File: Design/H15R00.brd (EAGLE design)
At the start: 34.6 x 30 mm, 21 parts, among them P1 HEXABIT_17.32_NO_P3_P6, U1 STM32F091CBU6, X1 XTALL_CSTCE8M00G52

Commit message: Finished schematics
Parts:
- added AO: 1751248, Hexabitz:CON-PHOENIX-350_1751248
- added C10, C11: 100nF, Hexabitz:C-0603
- added C12, C13: 100pF, Hexabitz:C-0603
- added C14, C15: 10pF, Hexabitz:C-0603
- added C16: 20nF, Hexabitz:C-0603
- added C17: 150pF, Hexabitz:C-0603
- added PWR: 1751251, con-phoenix-350:1751251
- added R4: 71.5R, Hexabitz:R-0603
- added R5: 24.9K, Hexabitz:R-0603
- added R6: 8.25K, Hexabitz:R-0603
- added R7: 12.4K, Hexabitz:R-0603
- added U2: OPA188, Hexabitz:DBV0005A_N
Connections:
- net UART1_RX renamed UART1_RX*
- net UART1_TX renamed UART1_TX*
- net UART2_RX renamed UART2_RX*
- net UART2_TX renamed UART2_TX*
- removed net UART6_RX: U1.P$15
- removed net UART6_TX: U1.P$14
- new net +15V: C11.1, C13.1, C14.1, PWR.3, U2.5
- new net -15V: C10.1, C12.1, C15.1, PWR.1, U2.2
- new net AGND: AO.2, C10.2, C12.2, C14.2, C15.2, C16.2, PWR.2, R7.2
- new net DAC_OUT: U1.P$14, U2.3
- new net N$1: AO.1, C16.1, R4.1
- new net N$10: R5.1
- new net N$11: P1.PAD_PU1
- new net N$12: P1.PAD_PU2
- new net N$13: P1.PAD_PU4
- new net N$14: P1.PAD_PD5
- new net N$15: P1.PAD_PD1
- new net N$16: P1.PAD_PD2
- new net N$17: P1.PAD_PD4
- new net N$18: P1.PAD_PU5
- new net N$2: C17.2, R4.2, U2.1
- new net N$8: C17.1, R5.2, R6.1, R7.1, U2.4
- new net VCC: R6.2
- net VSSA: now also C11.2, C13.2

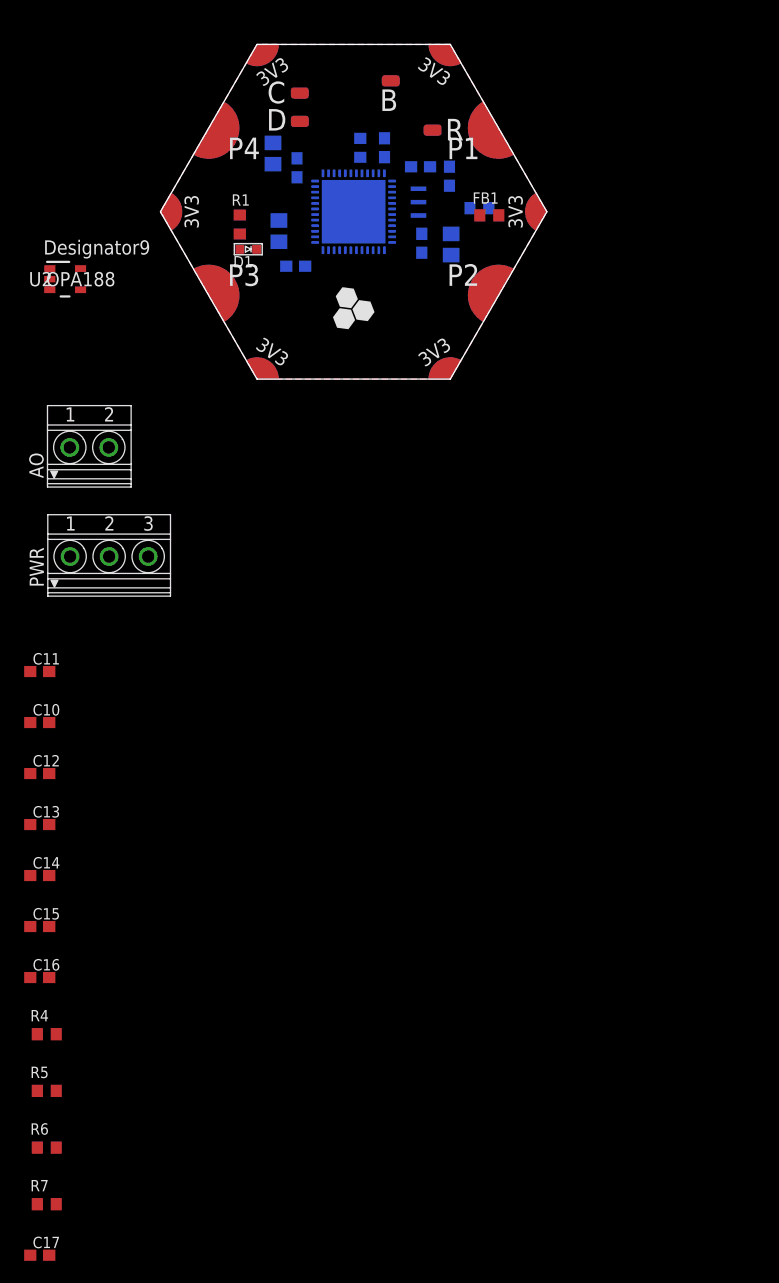
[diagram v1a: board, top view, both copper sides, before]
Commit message: Placed all components Routed analog part and most digital Added VSSA polygon
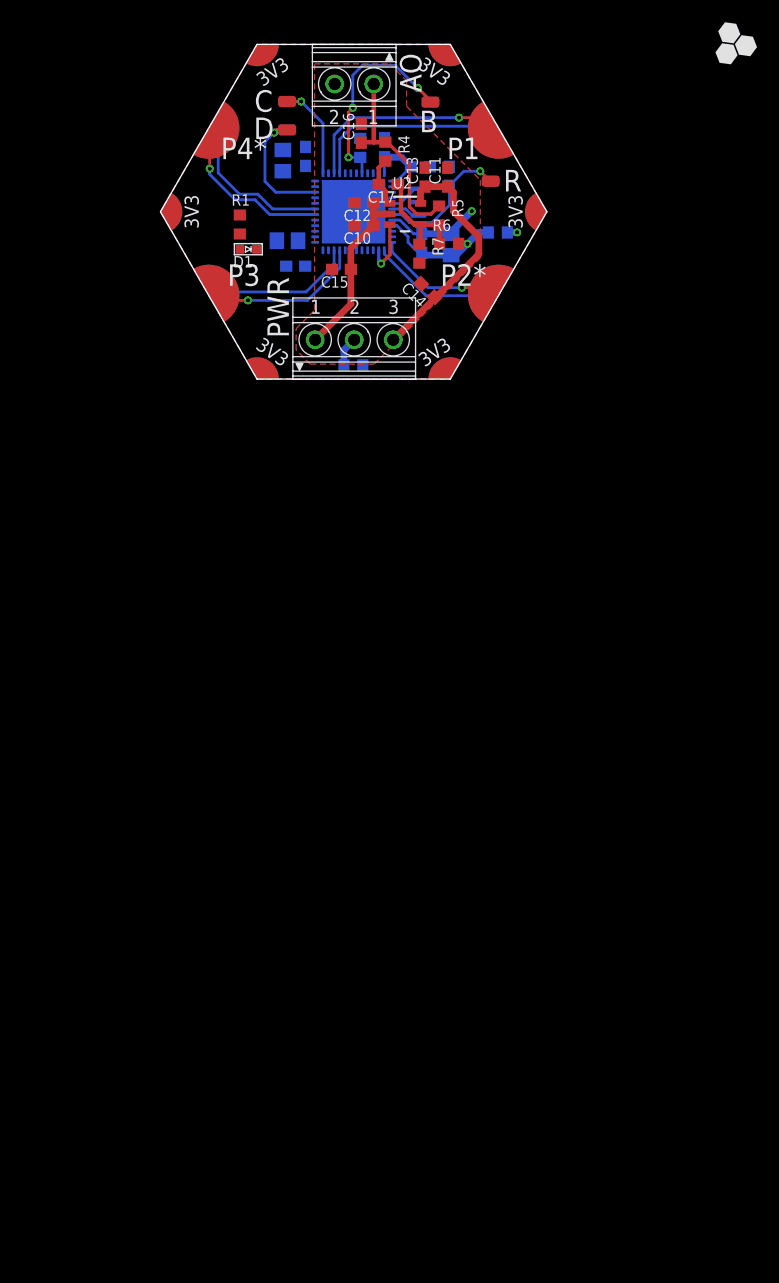
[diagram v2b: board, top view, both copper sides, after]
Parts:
- moved C17 101.0 mm to (37.7, 37.1), turned to 180 degrees
- moved R7 91.5 mm to (40.5, 30.9), turned to 270 degrees
- moved R6 88.7 mm to (43.2, 31.8)
- moved R5 86.0 mm to (42.3, 34.3), turned to 270 degrees
- moved R4 84.7 mm to (37.5, 40.0), turned to 270 degrees
- moved C16 81.0 mm to (35.3, 41.7), turned to 90 degrees
- moved C13 67.5 mm to (41.0, 37.7), turned to 90 degrees
- moved C15 64.8 mm to (33.5, 29.5), turned to 180 degrees
- moved C14 62.9 mm to (41.3, 27.6), turned to 135 degrees
- moved C12 58.9 mm to (35.6, 35.4), turned to 180 degrees
- moved C11 57.5 mm to (43.1, 37.7), turned to 90 degrees
- moved C10 53.2 mm to (35.6, 33.4), turned to 180 degrees
- moved AO 40.2 mm to (34.7, 46.0), turned to 180 degrees
- moved U2 31.0 mm to (39.2, 34.4)
- moved PWR 29.3 mm to (34.7, 23.2)
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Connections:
- removed net AGND: AO.2, C10.2, C12.2, C14.2, C15.2, C16.2, PWR.2, R7.2
- removed net N$10: R5.1
- removed net N$11: P1.PAD_PU1
- removed net N$12: P1.PAD_PU2
- removed net N$13: P1.PAD_PU4
- removed net N$14: P1.PAD_PD5
- removed net N$15: P1.PAD_PD1
- removed net N$16: P1.PAD_PD2
- removed net N$17: P1.PAD_PD4
- removed net N$18: P1.PAD_PU5
- removed net VCC: R6.2
- net N$1: now also R5.1
- net UART1_RX*: now also P1.PAD_PD5
- net UART1_TX*: now also P1.PAD_PU5
- net UART2_RX*: now also P1.PAD_PD2
- net UART2_TX*: now also P1.PAD_PU2
- net UART3_RX: now also P1.PAD_PD4
- net UART3_TX: now also P1.PAD_PU4
- net UART5_RX: now also P1.PAD_PD1
- net UART5_TX: now also P1.PAD_PU1
- net VDDA: now also R6.2
- net VSSA: now also AO.2, C10.2, C12.2, C14.2, C15.2, C16.2, PWR.2, R7.2
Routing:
- net +15V: track 0.00 -> 21.8 mm
- net B1: track 0.00 -> 20.6 mm, vias 0 -> 3
- net UART5_TX: track 0.00 -> 18.7 mm, vias 0 -> 1
- net N$1: track 0.00 -> 17.4 mm
- net UART5_RX: track 0.00 -> 17.4 mm
- net -15V: track 0.00 -> 15.9 mm
- net UART1_TX*: track 0.00 -> 15.0 mm, vias 0 -> 1
- net UART3_TX: track 0.00 -> 14.3 mm, vias 0 -> 1
- net UART1_RX*: track 0.00 -> 13.8 mm
- net R1: track 0.00 -> 13.7 mm, vias 0 -> 1
- net UART3_RX: track 0.00 -> 12.9 mm
- net N$7: track 0.00 -> 12.1 mm, vias 0 -> 1
- net UART2_RX*: track 0.00 -> 11.7 mm
- net VDDA: track 0.00 -> 11.7 mm, vias 0 -> 1
- net VSSA: track 0.00 -> 11.3 mm, vias 0 -> 1
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- added copper zone on layer 1, net VSSA
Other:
- board text added: "P2*"
- board text added: "P4*"
- board text removed: "P2"
- board text removed: "P4"

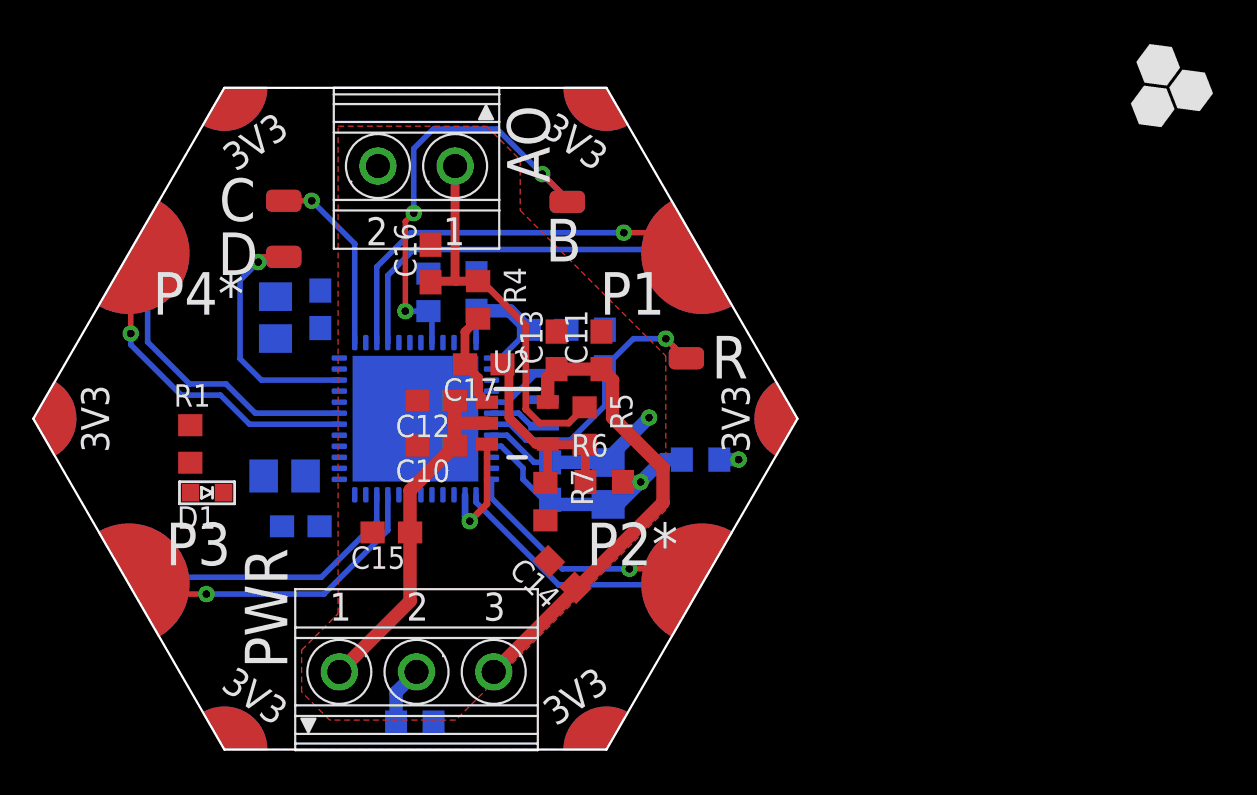
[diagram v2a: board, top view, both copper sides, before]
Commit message: Finished routing and silkscreen
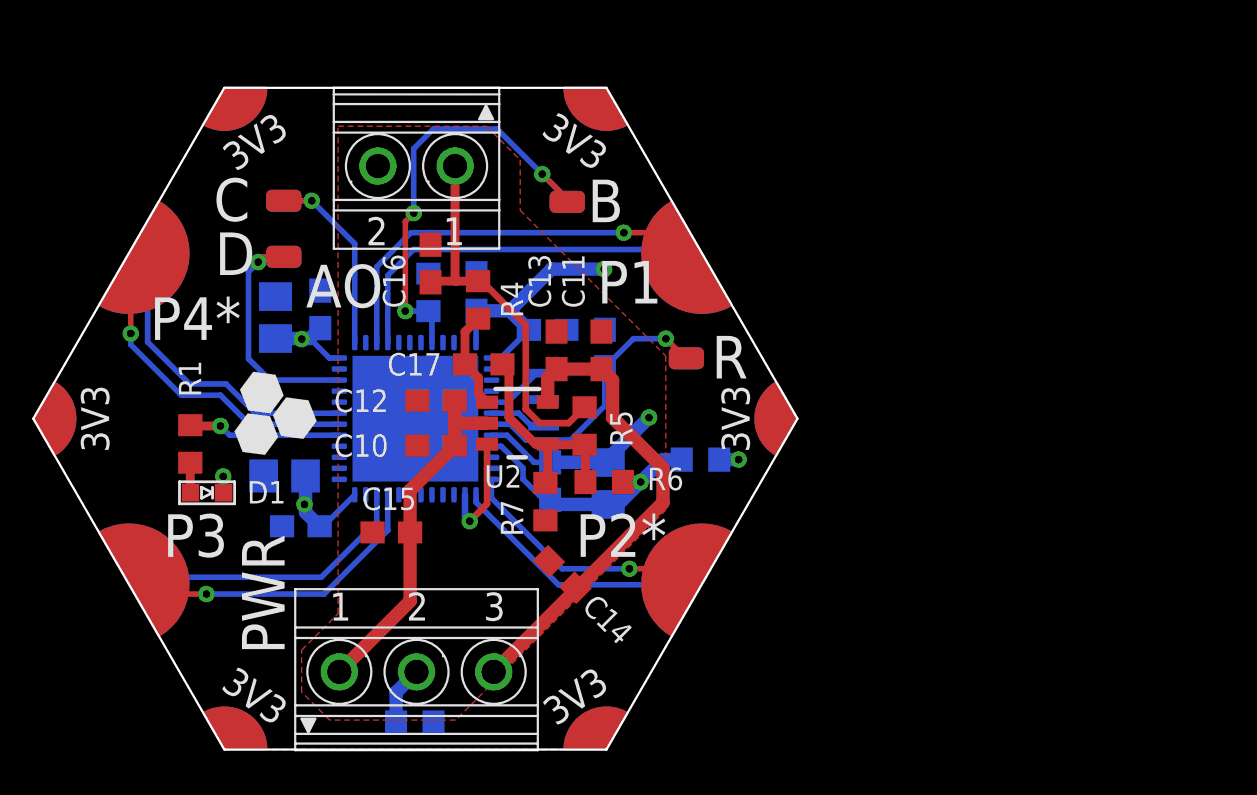
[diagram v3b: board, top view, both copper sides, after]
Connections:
- net GND: now also U1.P$15, U1.P$16, U1.P$17, U1.P$18, U1.P$19, U1.P$2, U1.P$20, U1.P$3, U1.P$32, U1.P$33, U1.P$38, U1.P$4, U1.P$45, U1.P$46
- net N$3: now also U1.P$29; no longer U1.P$32
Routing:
- net VDD: track 7.29 -> 21.0 mm, vias 1 -> 4
- net N$3: track 0.00 -> 6.94 mm, vias 0 -> 1
- net N$4: track 0.00 -> 1.37 mm
- net GND: track 0.00 -> 0.75 mm, vias 0 -> 1
- net N$7: track 12.1 -> 11.6 mm
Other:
- board text added: "+15V"
- board text added: "-10V..10V"
- board text added: "-15V"
- board text added: "AO"

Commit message: Solved DRC Generated gerber, drill, pick n place and schematics Generated BOM First release Ver 0
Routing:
- net VDD: track 21.0 -> 21.7 mm
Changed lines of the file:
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@@
 <attribute name="COMPTYPE" value="IC" x="39.243" y="34.417" size="1.778" layer="27" display="off"/>
 <attribute name="MANUFACTURER" value="Texas Instruments" x="39.243" y="34.417" size="1.778" layer="27" display="off"/>
+<attribute name="MFN" value="Texas Instruments" x="39.243" y="34.417" size="1.778" layer="27" display="off"/>
 <attribute name="MOUNTTYPE" value="SMT" x="39.243" y="34.417" size="1.778" layer="27" display="off"/>
+<attribute name="MPN" value="OPA188AIDBVR" x="39.243" y="34.417" size="1.778" layer="27" display="off"/>
 <attribute name="NAME" x="37.7444" y="31.496" size="1.016" layer="25" rot="SR0"/>
+<attribute name="OCTOPART_URL" value="https://octopart.com/opa188aidbvr-texas+instruments-27810397?r=sp&amp;s=zwpAzK6tSwu39ID1-8lLKg" x="39.243" y="34.417" size="1.778" layer="27" display="off"/>
 <attribute name="PACKAGEREFERENCE" value="DBV0005A" x="39.243" y="34.417" size="1.778" layer="27" display="off"/>
 <attribute name="PARTNUMBER" value="OPA188AIDBVR" x="39.243" y="34.417" size="1.778" layer="27" display="off"/>
@@
 <attribute name="NAME" x="38.493190625" y="30.94939375" size="1.016" layer="25" rot="R270"/>
 <attribute name="OCTOPART_URL" value="https://octopart.com/era-3aeb1242v-panasonic-55639351?r=sp&amp;s=K0xQjqOwSGaT1tqbXnh0hg" x="40.513" y="30.861" size="1.778" layer="27" rot="R270" display="off"/>
-<attribute name="RESISTANCE" value="12.4 Ohm" x="40.513" y="30.861" size="1.778" layer="27" rot="R270" display="off"/>
+<attribute name="RESISTANCE" value="12.4 kOhm" x="40.513" y="30.861" size="1.778" layer="27" rot="R270" display="off"/>
 <attribute name="TOLERANCE" value="0.1%" x="40.513" y="30.861" size="1.778" layer="27" rot="R270" display="off"/>
 <attribute name="VALUE" x="38.622984375" y="32.398971875" size="1.016" layer="27" rot="R270"/>
@@
 <wire x1="31.8702" y1="31.17019375" x2="30.44035625" y2="29.74035" width="0.254" layer="16"/>
 <wire x1="30.44035625" y1="29.74035" x2="30.274375" y2="29.74035" width="0.254" layer="16"/>
-<wire x1="30.274375" y1="29.74035" x2="29.638284375" y2="30.376440625" width="0.6096" layer="16"/>
-<wire x1="29.638284375" y1="30.376440625" x2="29.638284375" y2="32.022790625" width="0.6096" layer="16"/>
-<wire x1="28.276303125" y1="38.253853125" x2="29.8359" y2="38.253853125" width="0.6096" layer="16"/>
 <wire x1="29.8359" y1="38.253853125" x2="30.3095625" y2="38.727515625" width="0.6096" layer="16"/>
 <wire x1="31.17019375" y1="37.3702" x2="30.719553125" y2="37.3702" width="0.254" layer="16"/>
@@
 <wire x1="40.7904875" y1="41.402" x2="43.18" y2="41.402" width="0.6096" layer="16"/>
 <via x="43.18" y="41.402" extent="1-16" drill="0.35"/>
-<wire x1="29.464" y1="38.227" x2="29.8359" y2="38.253853125" width="0" layer="19" extent="16-16"/>
-<wire x1="29.638284375" y1="30.376440625" x2="29.591" y2="30.734" width="0" layer="19" extent="16-16"/>
+<wire x1="30.3095625" y1="38.727515625" x2="29.809046875" y2="38.227" width="0.6096" layer="16"/>
+<wire x1="29.809046875" y1="38.227" x2="29.464" y2="38.227" width="0.6096" layer="16"/>
+<wire x1="29.464" y1="38.227" x2="28.30315625" y2="38.227" width="0.6096" layer="16"/>
+<wire x1="28.30315625" y1="38.227" x2="28.276303125" y2="38.253853125" width="0.6096" layer="16"/>
+<wire x1="29.591" y1="30.734" x2="29.591" y2="30.423725" width="0.6096" layer="16"/>
+<wire x1="29.591" y1="30.423725" x2="30.274375" y2="29.74035" width="0.6096" layer="16"/>
+<wire x1="29.591" y1="30.734" x2="29.591" y2="31.97550625" width="0.6096" layer="16"/>
+<wire x1="29.591" y1="31.97550625" x2="29.638284375" y2="32.022790625" width="0.6096" layer="16"/>
 </signal>
 <signal name="UART3_TX">
@@
 <wire x1="40.618" y1="36.466" x2="41.021" y2="36.869" width="0.6096" layer="1"/>
 <wire x1="41.021" y1="36.869" x2="43.053" y2="36.869" width="0.6096" layer="1"/>
-<wire x1="38.171" y1="23.141" x2="45.847" y2="30.817" width="0.6096" layer="1"/>
-<wire x1="45.847" y1="30.817" x2="45.847" y2="32.385" width="0.6096" layer="1"/>
+<wire x1="45.847" y1="32.385" x2="45.847" y2="30.817" width="0.6096" layer="1"/>
 <wire x1="45.847" y1="32.385" x2="43.561" y2="34.671" width="0.6096" layer="1"/>
 <wire x1="43.053" y1="36.869" x2="43.561" y2="36.361" width="0.6096" layer="1"/>
 <wire x1="43.561" y1="36.361" x2="43.561" y2="34.671" width="0.6096" layer="1"/>
-<wire x1="38.171" y1="23.141" x2="41.876040625" y2="26.95795625" width="0" layer="19" extent="1-1"/>
+<wire x1="45.847" y1="30.817" x2="41.98795625" y2="26.95795625" width="0.6096" layer="1"/>
+<wire x1="41.98795625" y1="26.95795625" x2="41.876040625" y2="26.95795625" width="0.6096" layer="1"/>
+<wire x1="41.876040625" y1="26.95795625" x2="38.171" y2="23.252915625" width="0.6096" layer="1"/>
+<wire x1="38.171" y1="23.252915625" x2="38.171" y2="23.141" width="0.6096" layer="1"/>
 </signal>
 <signal name="-15V">
@@
 <mfgpreviewcolor name="substratecolor" color="0xFF786E46"/>
 </mfgpreviewcolors>
+<errors>
+</errors>
 </board>
 </drawing>
